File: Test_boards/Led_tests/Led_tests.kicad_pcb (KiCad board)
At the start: 2 copper layers, 25 x 20 mm, 0 parts

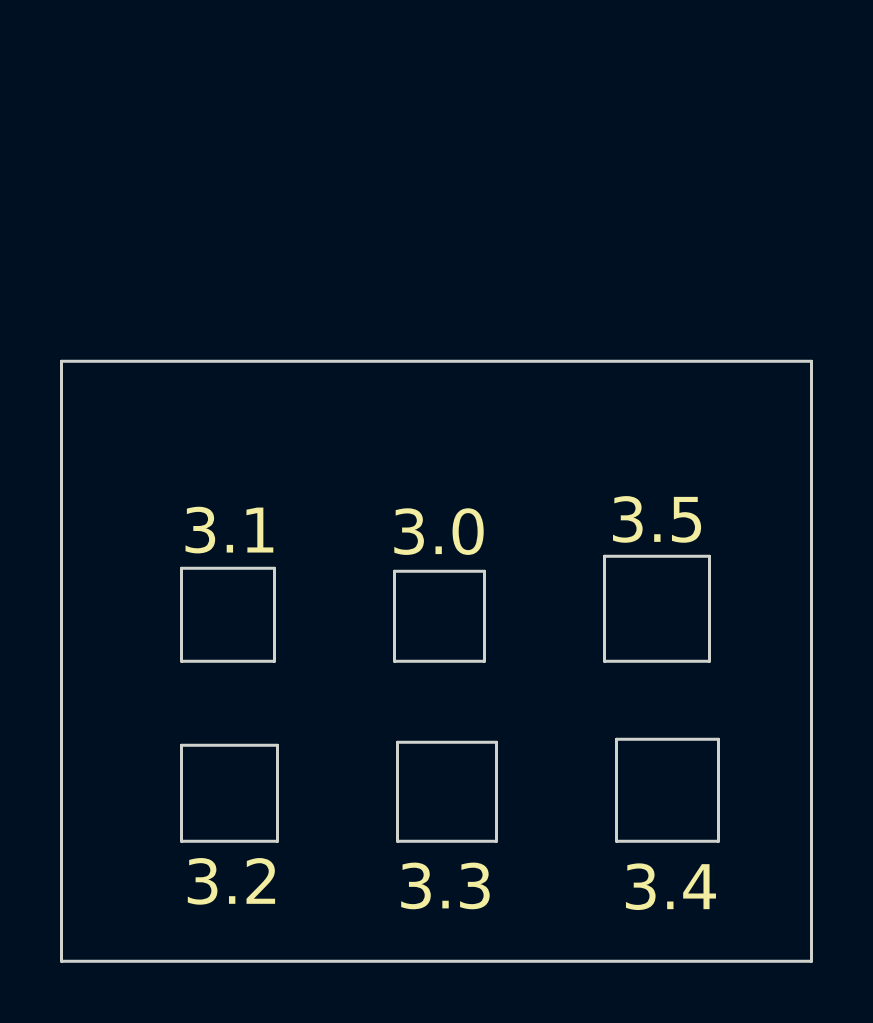
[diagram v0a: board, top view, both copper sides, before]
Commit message: Completed LED castellated hole test board
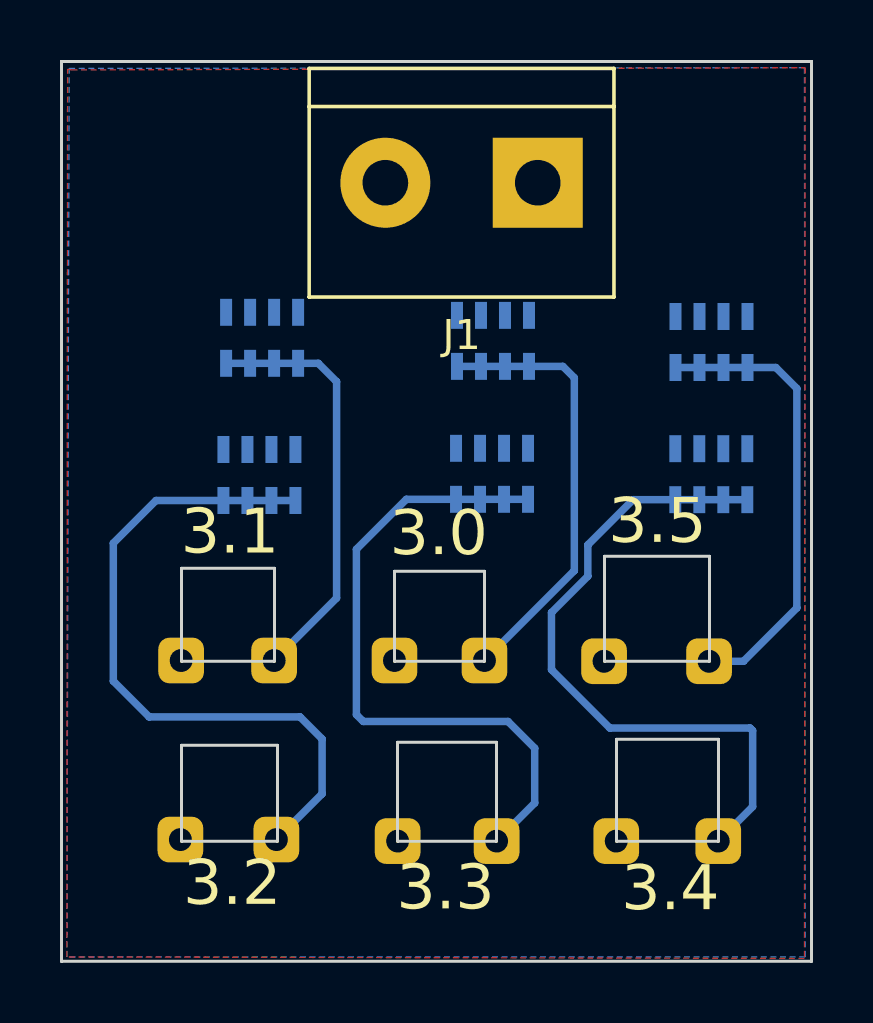
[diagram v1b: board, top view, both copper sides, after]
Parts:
- added D1: 3.0mm, LTST-S110KGKT_castellated:LTST-S110KGKT_castellated_3.0mm, F.Cu at (39.0, 31.5)
- added D2: 3.1mm, LTST-S110KGKT_castellated:LTST-S110KGKT_castellated_3.1mm, F.Cu at (32.0, 31.5)
- added D3: 3.2mm, LTST-S110KGKT_castellated:LTST-S110KGKT_castellated_3.2mm, F.Cu at (32.0, 37.5)
- added D4: 3.3mm, LTST-S110KGKT_castellated:LTST-S110KGKT_castellated_3.3mm, F.Cu at (39.3, 37.5)
- added D5: 3.4mm, LTST-S110KGKT_castellated:LTST-S110KGKT_castellated_3.4mm, F.Cu at (46.6, 37.5)
- added D6: 3.5mm, LTST-S110KGKT_castellated:LTST-S110KGKT_castellated_3.5mm, F.Cu at (46.3, 31.5)
- added J1: Screw_Terminal_01x02, TerminalBlock:TerminalBlock_bornier-2_P5.08mm, F.Cu at (42.3, 15.6)
- added RN1: R_Pack04, Resistor_SMD:R_Array_Concave_4x0603, B.Cu at (40.8, 20.8)
- added RN2: R_Pack04, Resistor_SMD:R_Array_Concave_4x0603, B.Cu at (33.1, 20.7)
- added RN3: R_Pack04, Resistor_SMD:R_Array_Concave_4x0603, B.Cu at (33.0, 25.3)
- added RN4: R_Pack04, Resistor_SMD:R_Array_Concave_4x0603, B.Cu at (40.8, 25.3)
- added RN5: R_Pack04, Resistor_SMD:R_Array_Concave_4x0603, B.Cu at (48.1, 25.3)
- added RN6: R_Pack04, Resistor_SMD:R_Array_Concave_4x0603, B.Cu at (48.1, 20.9)
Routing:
- net Net-(D3-Pad2): track 0.00 -> 22.4 mm
- net Net-(D4-Pad2): track 0.00 -> 21.8 mm
- net Net-(D5-Pad2): track 0.00 -> 21.8 mm
- net Net-(D6-Pad2): track 0.00 -> 14.9 mm
- net Net-(D1-Pad2): track 0.00 -> 14.2 mm
- net Net-(D2-Pad2): track 0.00 -> 13.5 mm
- added copper zone on F.Cu, net GND
- added copper zone on B.Cu, net Net-(J1-Pad2)
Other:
- board size 25 x 20 mm -> 25 x 30 mm
